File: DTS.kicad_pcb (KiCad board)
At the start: 2 copper layers, 15 parts, among them J1 Conn_01x03, J2 Conn_01x03, J3 Conn_01x03, U1 4081, U10 4081, U11 4081, U12 4071, U2 4081, U3 4069, U4 4071, U5 4069, U6 4081, U7 4081, U8 4071, U9 4069

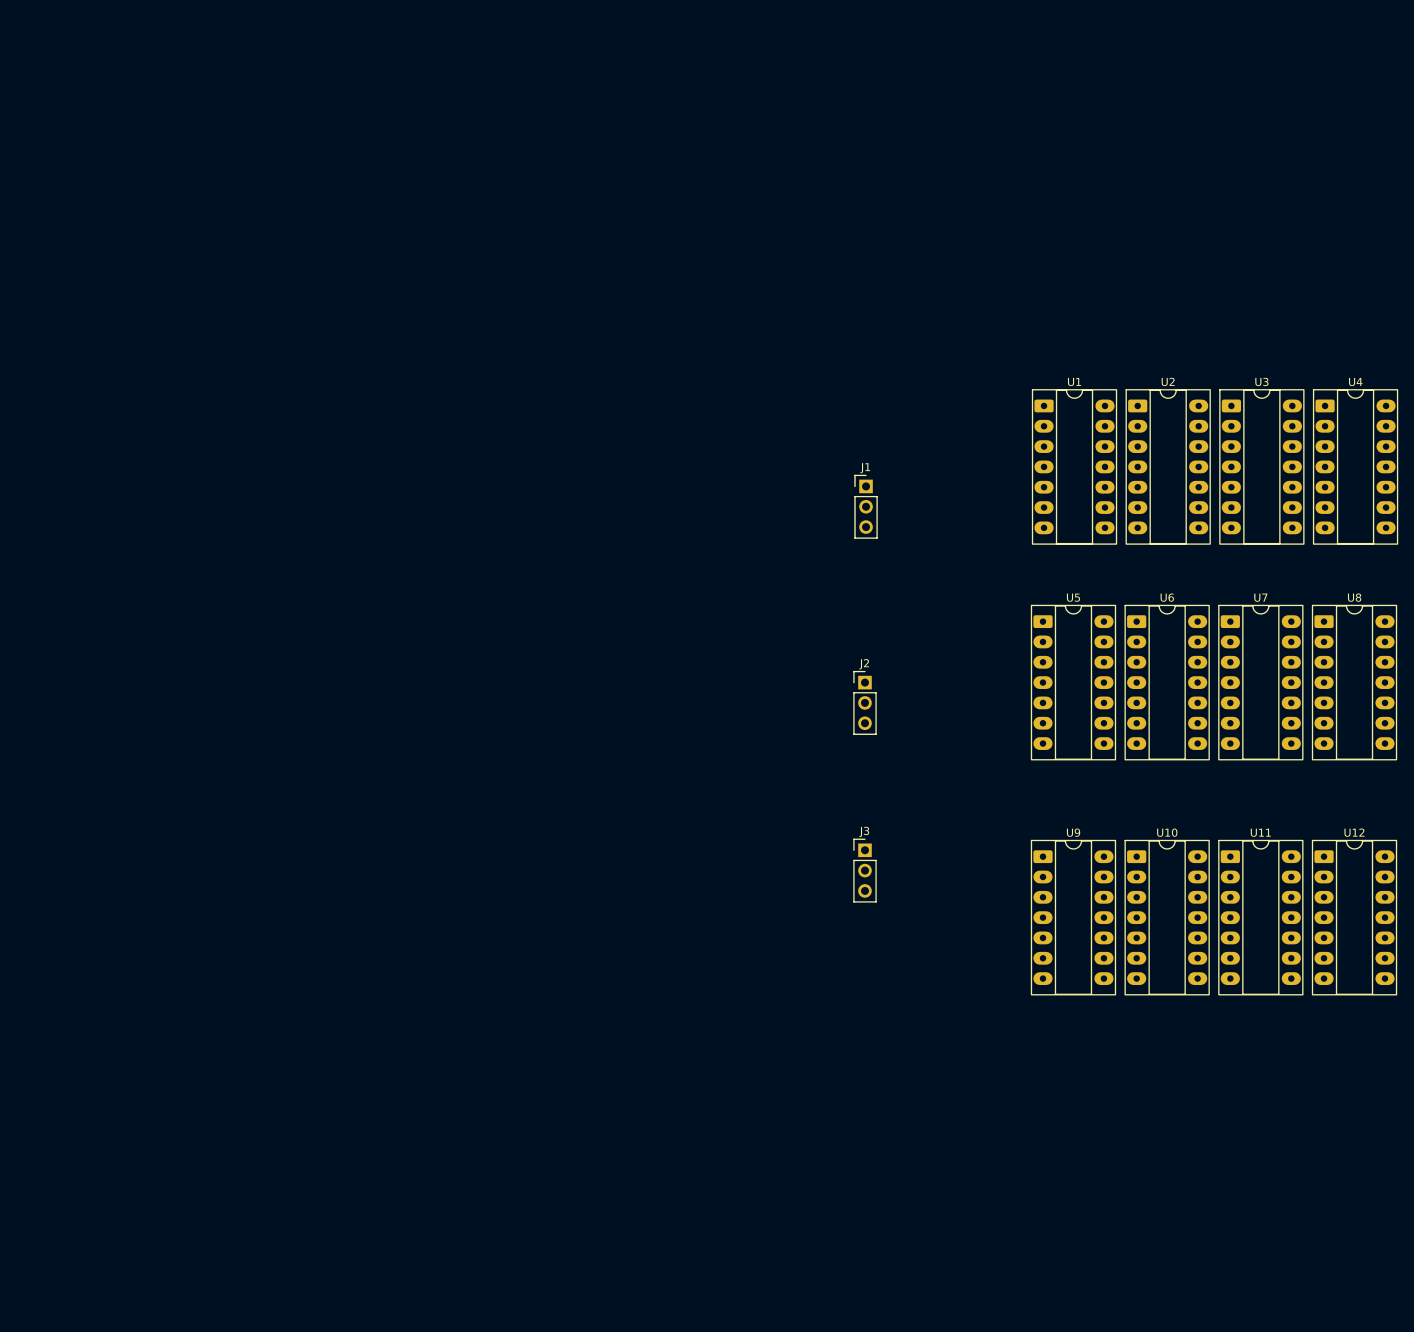
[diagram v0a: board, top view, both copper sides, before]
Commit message: Add files via upload
Added 3 bits 2:1 and 6 bits 4:1 multiplexer
Added minus operation
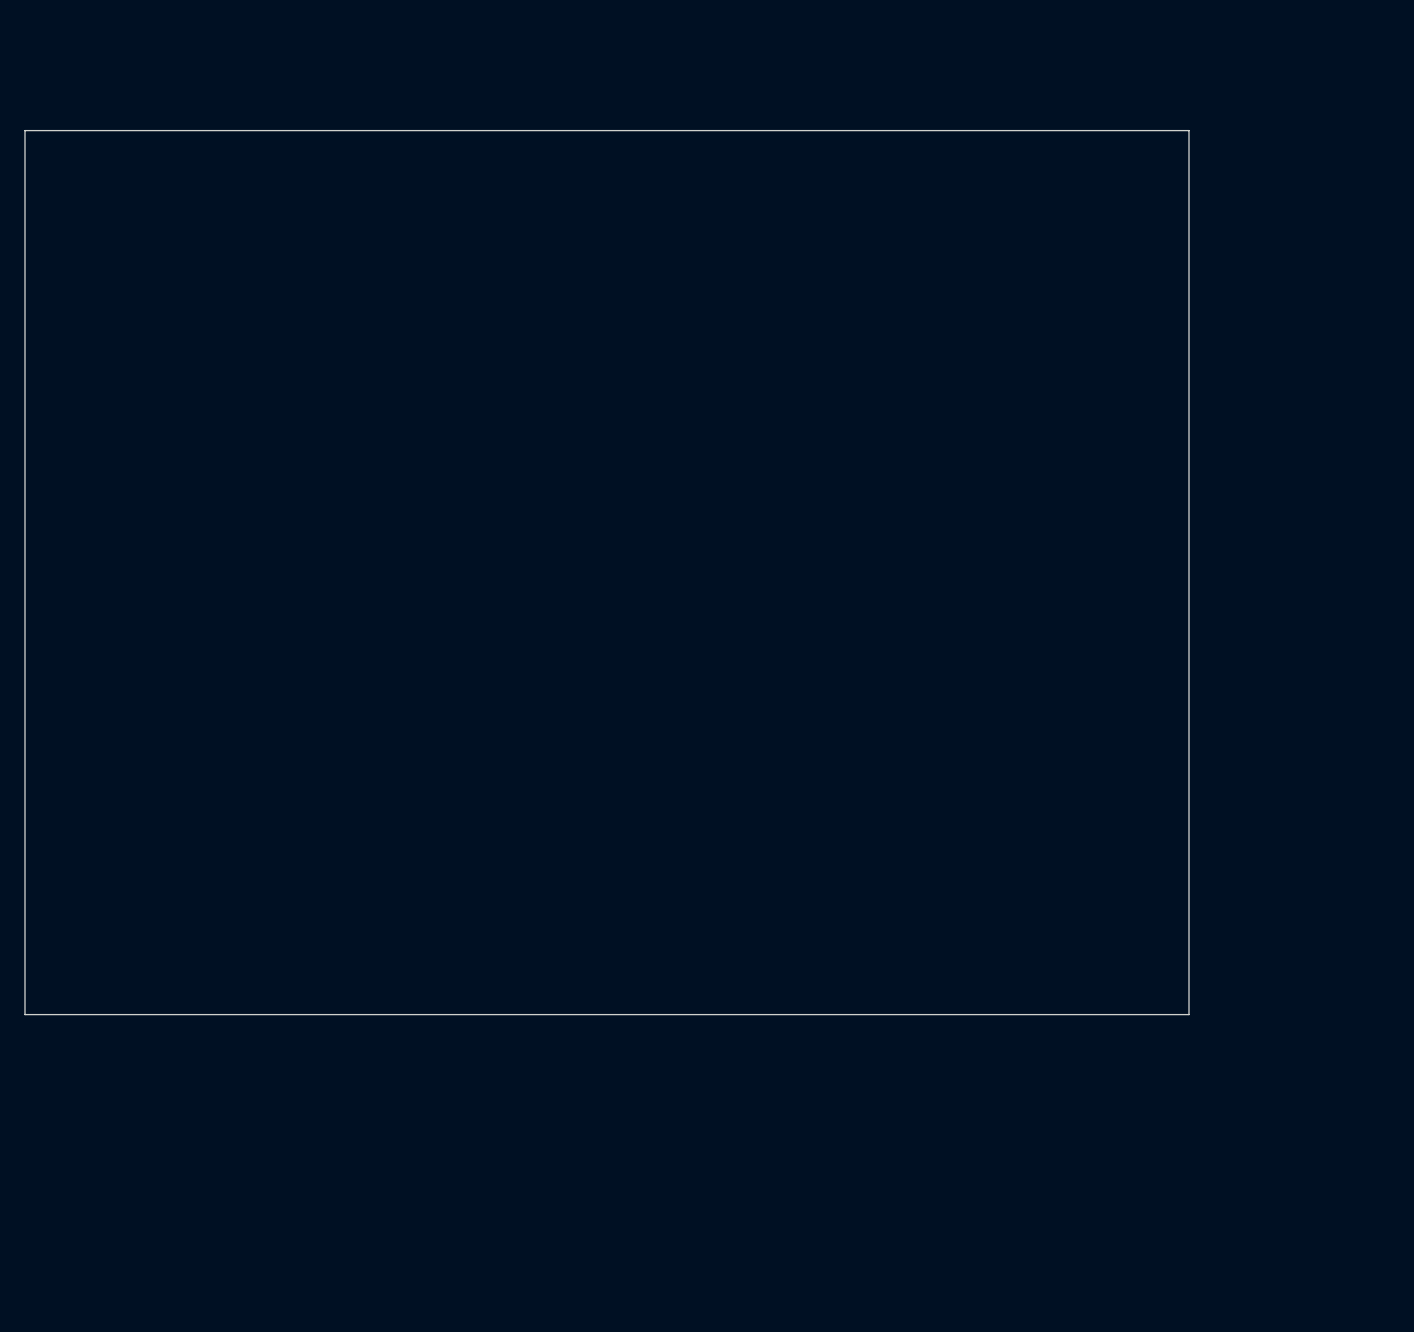
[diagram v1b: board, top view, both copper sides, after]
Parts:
- removed J1, J2, J3: Conn_01x03, Connector_PinHeader_2.54mm:PinHeader_1x03_P2.54mm_Vertical
- removed U1, U10, U11, U2, U6, U7: 4081, Package_DIP:CERDIP-14_W7.62mm_SideBrazed_LongPads_Socket
- removed U12, U4, U8: 4071, Package_DIP:CERDIP-14_W7.62mm_SideBrazed_LongPads_Socket
- removed U3, U5, U9: 4069, Package_DIP:CERDIP-14_W7.62mm_SideBrazed_LongPads_Socket
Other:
- board outline added: 145.5 x 110.5 mm

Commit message: Add files via upload
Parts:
- added C1: 0.22u, Capacitor_THT:C_Rect_L7.0mm_W2.0mm_P5.00mm, F.Cu at (124.4, 173.2)
- added C2: 0.1u, Capacitor_THT:C_Rect_L7.0mm_W2.0mm_P5.00mm, F.Cu at (134.9, 171.2)
- added J1: Conn_01x02_Pin, Connector_PinHeader_2.54mm:PinHeader_1x02_P2.54mm_Vertical, F.Cu at (112.4, 174.4)
- added J2: Conn_01x06_Pin, Connector_PinHeader_2.54mm:PinHeader_1x06_P2.54mm_Vertical, F.Cu at (31.2, 53.5)
- added J3: Conn_01x02_Pin, Connector_PinHeader_2.54mm:PinHeader_1x02_P2.54mm_Vertical, F.Cu at (31.6, 78.2)
- added J4: Conn_01x06_Pin, Connector_PinHeader_2.54mm:PinHeader_1x06_P2.54mm_Vertical, F.Cu at (31.2, 128.2)
- added SW1: SW_DIP_x01, Connector_PinSocket_2.54mm:PinSocket_1x02_P2.54mm_Vertical, F.Cu at (117.4, 174.2)
- added U1: 4081, Package_DIP:CERDIP-14_W7.62mm_SideBrazed_LongPads_Socket, F.Cu at (122.8, 28.4)
- added U10: 4071, Package_DIP:CERDIP-14_W7.62mm_SideBrazed_LongPads_Socket, F.Cu at (82.3, 28.9)
- added U11: 4081, Package_DIP:CERDIP-14_W7.62mm_SideBrazed_LongPads_Socket, F.Cu at (66.5, 124.6)
- added U12: 4081, Package_DIP:CERDIP-14_W7.62mm_SideBrazed_LongPads_Socket, F.Cu at (53.3, 52.0)
- added U13: 4071, Package_DIP:CERDIP-14_W7.62mm_SideBrazed_LongPads_Socket, F.Cu at (67.4, 100.9)
- added U14: 4069, Package_DIP:CERDIP-14_W7.62mm_SideBrazed_LongPads_Socket, F.Cu at (95.9, 51.8)
- added U15: 4081, Package_DIP:CERDIP-14_W7.62mm_SideBrazed_LongPads_Socket, F.Cu at (40.4, 148.1)
- added U16: 4081, Package_DIP:CERDIP-14_W7.62mm_SideBrazed_LongPads_Socket, F.Cu at (68.3, 52.1)
- added U17: 4071, Package_DIP:CERDIP-14_W7.62mm_SideBrazed_LongPads_Socket, F.Cu at (94.8, 148.9)
- added U18: 4069, Package_DIP:CERDIP-14_W7.62mm_SideBrazed_LongPads_Socket, F.Cu at (53.9, 75.2)
- added U19: 4081, Package_DIP:CERDIP-14_W7.62mm_SideBrazed_LongPads_Socket, F.Cu at (80.3, 148.9)
- added U2: 4081, Package_DIP:CERDIP-14_W7.62mm_SideBrazed_LongPads_Socket, F.Cu at (39.9, 52.6)
- added U20: 4081, Package_DIP:CERDIP-14_W7.62mm_SideBrazed_LongPads_Socket, F.Cu at (67.9, 75.5)
- added U21: 4071, Package_DIP:CERDIP-14_W7.62mm_SideBrazed_LongPads_Socket, F.Cu at (122.3, 149.9)
- added U22: 4069, Package_DIP:CERDIP-14_W7.62mm_SideBrazed_LongPads_Socket, F.Cu at (81.4, 100.1)
- added U23: 4081, Package_DIP:CERDIP-14_W7.62mm_SideBrazed_LongPads_Socket, F.Cu at (121.8, 74.9)
- added U24: 4081, Package_DIP:CERDIP-14_W7.62mm_SideBrazed_LongPads_Socket, F.Cu at (39.9, 75.4)
- added U25: 4081, Package_DIP:CERDIP-14_W7.62mm_SideBrazed_LongPads_Socket, F.Cu at (95.3, 101.4)
- added U26: 4071, Package_DIP:CERDIP-14_W7.62mm_SideBrazed_LongPads_Socket, F.Cu at (122.4, 101.4)
- added U27: 4069, Package_DIP:CERDIP-14_W7.62mm_SideBrazed_LongPads_Socket, F.Cu at (108.8, 51.5)
- added U28: 4081, Package_DIP:CERDIP-14_W7.62mm_SideBrazed_LongPads_Socket, F.Cu at (135.3, 101.9)
- added U29: 4081, Package_DIP:CERDIP-14_W7.62mm_SideBrazed_LongPads_Socket, F.Cu at (54.0, 100.7)
- added U3: 4071, Package_DIP:CERDIP-14_W7.62mm_SideBrazed_LongPads_Socket, F.Cu at (53.9, 124.6)
- added U30: 4081, Package_DIP:CERDIP-14_W7.62mm_SideBrazed_LongPads_Socket, F.Cu at (94.9, 75.1)
- added U31: 4071, Package_DIP:CERDIP-14_W7.62mm_SideBrazed_LongPads_Socket, F.Cu at (82.4, 52.0)
- added U32: 4069, Package_DIP:CERDIP-14_W7.62mm_SideBrazed_LongPads_Socket, F.Cu at (94.3, 125.0)
- added U34: 4081, Package_DIP:CERDIP-14_W7.62mm_SideBrazed_LongPads_Socket, F.Cu at (39.9, 100.7)
- added U35: 4081, Package_DIP:CERDIP-14_W7.62mm_SideBrazed_LongPads_Socket, F.Cu at (79.8, 124.9)
- added U36: 4071, Package_DIP:CERDIP-14_W7.62mm_SideBrazed_LongPads_Socket, F.Cu at (82.4, 75.1)
- added U37: 4069, Package_DIP:CERDIP-14_W7.62mm_SideBrazed_LongPads_Socket, F.Cu at (52.8, 28.4)
- added U38: 4081, Package_DIP:CERDIP-14_W7.62mm_SideBrazed_LongPads_Socket, F.Cu at (107.8, 125.4)
- added U39: 4081, Package_DIP:CERDIP-14_W7.62mm_SideBrazed_LongPads_Socket, F.Cu at (135.3, 124.9)
- added U4: 4069, Package_DIP:CERDIP-14_W7.62mm_SideBrazed_LongPads_Socket, F.Cu at (40.0, 124.9)
- added U40: 4071, Package_DIP:CERDIP-14_W7.62mm_SideBrazed_LongPads_Socket, F.Cu at (109.3, 101.4)
- added U41: 4081, Package_DIP:CERDIP-14_W7.62mm_SideBrazed_LongPads_Socket, F.Cu at (107.3, 148.9)
- added U42: 4081, Package_DIP:CERDIP-14_W7.62mm_SideBrazed_LongPads_Socket, F.Cu at (135.3, 75.0)
- added U43: 4071, Package_DIP:CERDIP-14_W7.62mm_SideBrazed_LongPads_Socket, F.Cu at (134.8, 51.5)
- added U44: 4081, Package_DIP:CERDIP-14_W7.62mm_SideBrazed_LongPads_Socket, F.Cu at (122.3, 125.3)
- added U45: 4081, Package_DIP:CERDIP-14_W7.62mm_SideBrazed_LongPads_Socket, F.Cu at (135.3, 29.0)
- added U46: 4071, Package_DIP:CERDIP-14_W7.62mm_SideBrazed_LongPads_Socket, F.Cu at (122.3, 50.5)
- added U47: 4081, Package_DIP:CERDIP-14_W7.62mm_SideBrazed_LongPads_Socket, F.Cu at (109.3, 74.9)
- added U48: 4081, Package_DIP:CERDIP-14_W7.62mm_SideBrazed_LongPads_Socket, F.Cu at (109.8, 28.5)
- added U49: LM7805_TO220, Package_TO_SOT_THT:TO-220-3_Vertical, F.Cu at (129.9, 176.2)
- added U5: 4069, Package_DIP:CERDIP-14_W7.62mm_SideBrazed_LongPads_Socket, F.Cu at (67.8, 28.5)
- added U6: 4081, Package_DIP:CERDIP-14_W7.62mm_SideBrazed_LongPads_Socket, F.Cu at (95.8, 30.4)
- added U7: 4081, Package_DIP:CERDIP-14_W7.62mm_SideBrazed_LongPads_Socket, F.Cu at (46.9, 45.6)
- added U8: 4071, Package_DIP:CERDIP-14_W7.62mm_SideBrazed_LongPads_Socket, F.Cu at (53.5, 148.6)
- added U9: 4069, Package_DIP:CERDIP-14_W7.62mm_SideBrazed_LongPads_Socket, F.Cu at (67.3, 148.9)
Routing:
- net GND: track 0.00 -> 857.9 mm
- net VCC: track 0.00 -> 812.4 mm, vias 0 -> 1
- net ctrl_out0: track 0.00 -> 403.9 mm, vias 0 -> 6
- net y3: track 0.00 -> 263.7 mm, vias 0 -> 3
- net xor3: track 0.00 -> 231.8 mm, vias 0 -> 4
- net /Multiplier/(A1B2)': track 0.00 -> 212.7 mm, vias 0 -> 3
- net ctrl_out1: track 0.00 -> 205.6 mm, vias 0 -> 1
- net x3: track 0.00 -> 196.3 mm, vias 0 -> 1
- net x2: track 0.00 -> 184.0 mm
- net /Multiplier/(A0B2)': track 0.00 -> 178.1 mm, vias 0 -> 8
- net /Multiplier/cout3: track 0.00 -> 173.3 mm
- net /Multiplexer_6b1/i0_5: track 0.00 -> 164.7 mm, vias 0 -> 3
- net s3: track 0.00 -> 152.4 mm, vias 0 -> 3
- net /Multiplier/A2B2: track 0.00 -> 145.8 mm, vias 0 -> 1
- net x1: track 0.00 -> 140.5 mm
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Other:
- board size 145.5 x 110.5 mm -> 122.4 x 162.4 mm
